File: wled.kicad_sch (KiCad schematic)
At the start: 12 parts, among them J0 Screw_Terminal_01x02, J1 Signal_Output_01, J3 1Wire_output_02, J4 1Wire_output_01, J5 I2C_output_01, SW1 Button_01, SW2 Button_Reset, U1 NodeMCU_1.0_(ESP-12E)

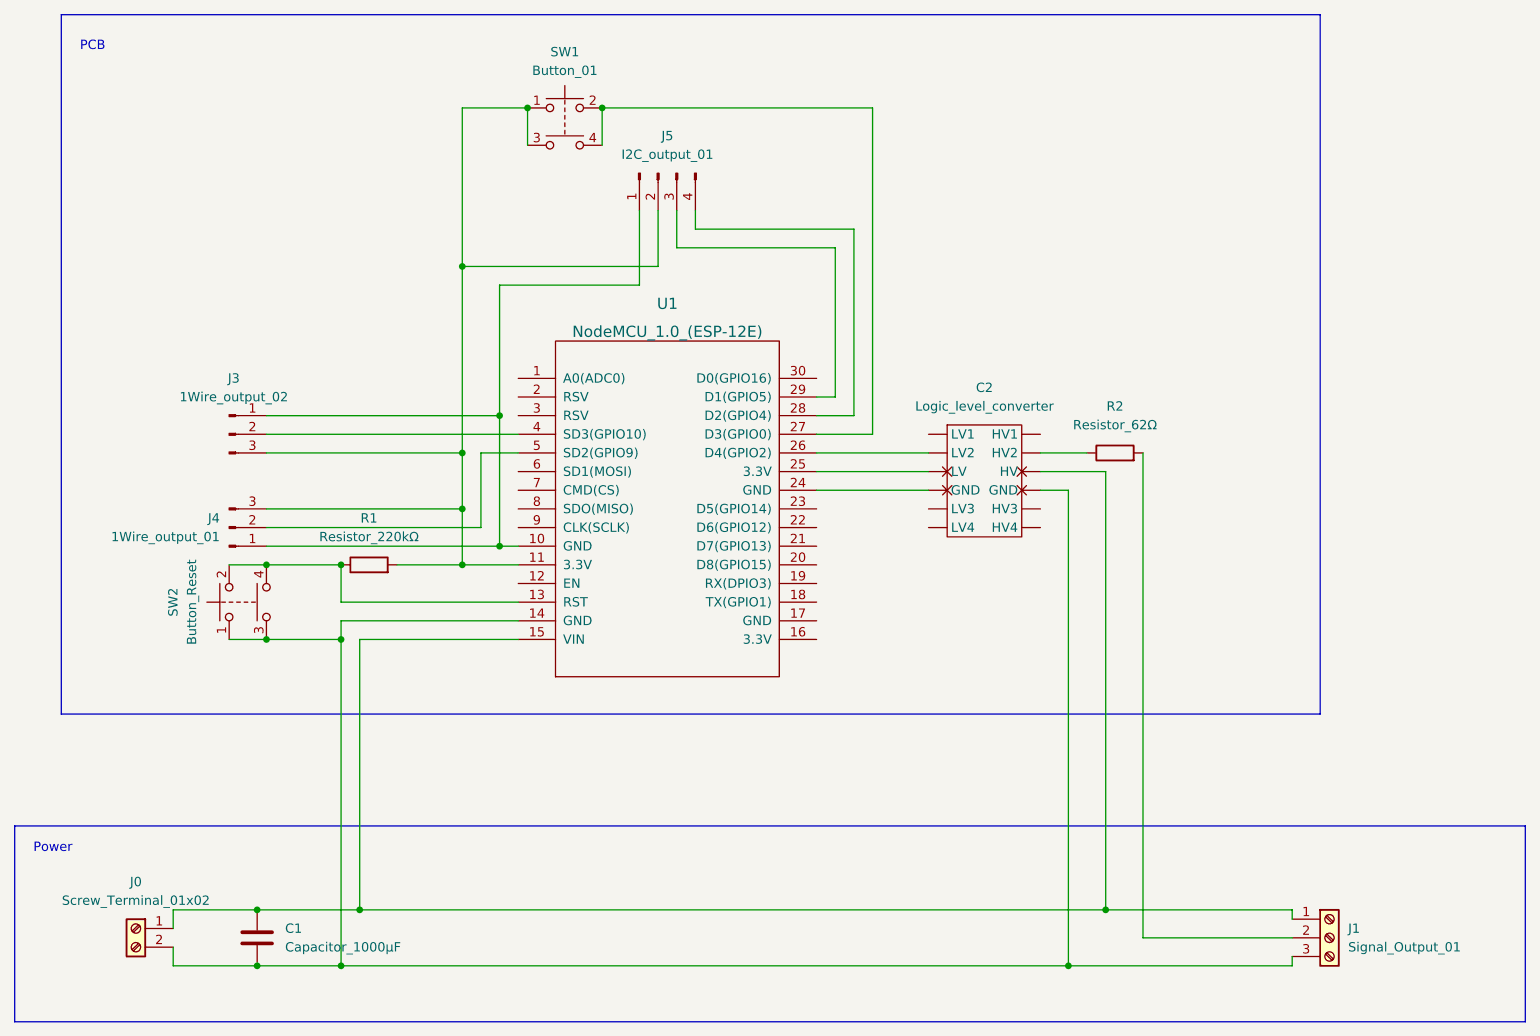
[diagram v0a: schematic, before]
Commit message: feat: Updated PCB design
This is a Release Candidate version of the board. It still has some issues, and they will be fixed in the next commit
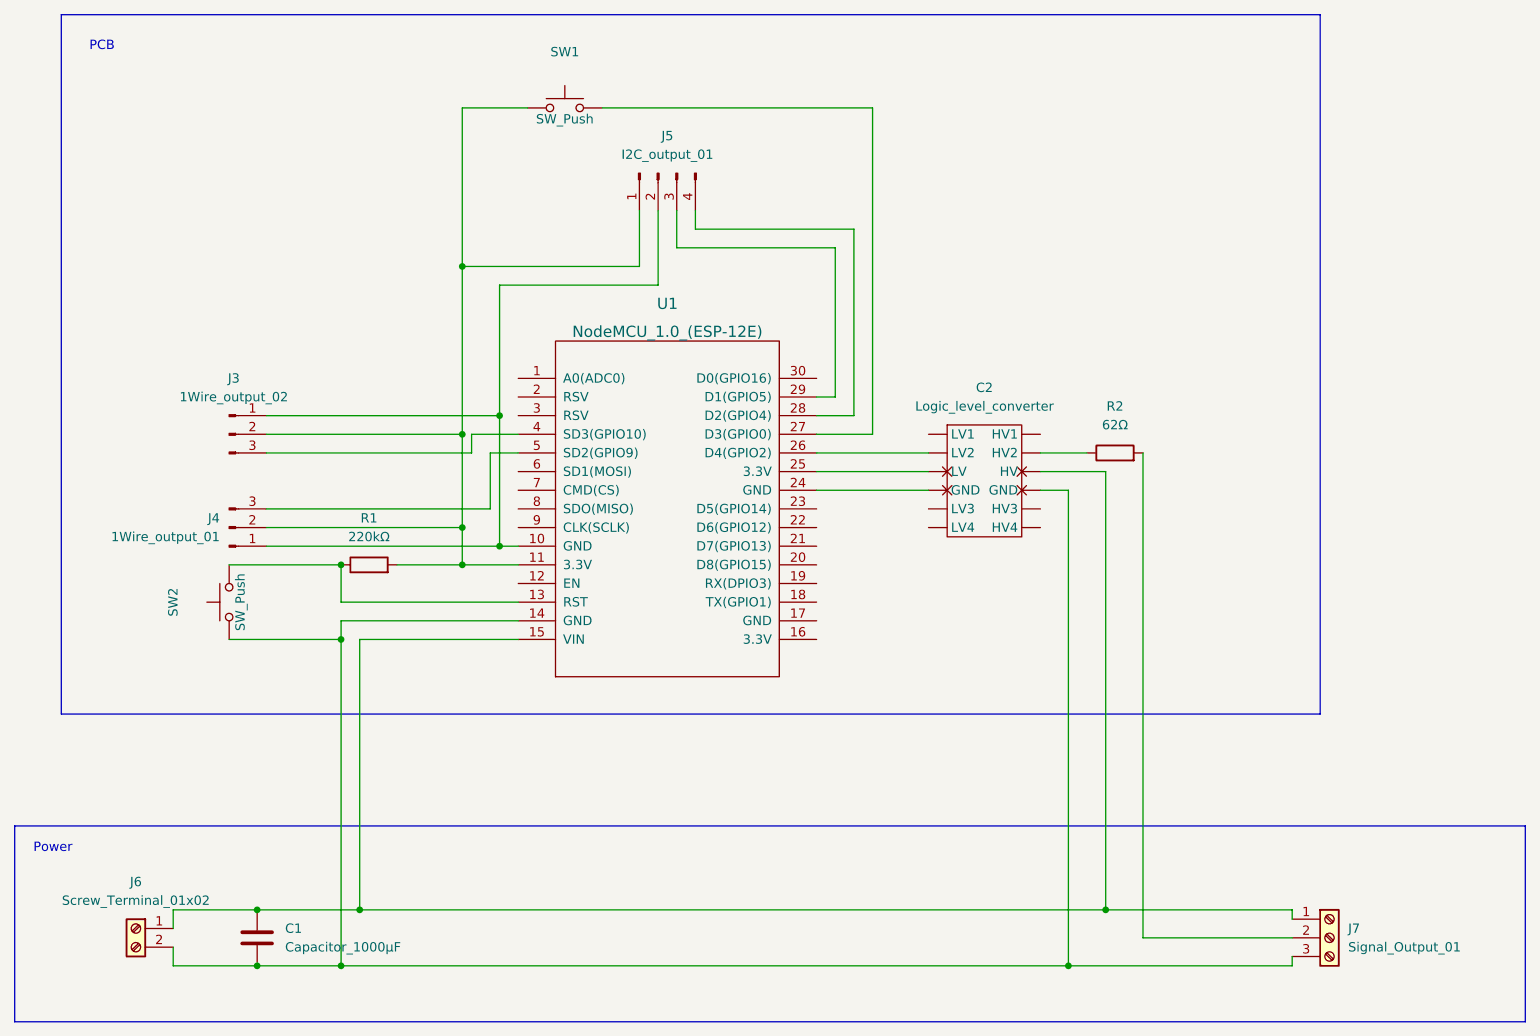
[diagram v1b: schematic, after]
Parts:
- C1: now left out of the parts list
- J6: renamed from J0; now left out of the parts list
- J7: renamed from J1; now left out of the parts list
- R1: value Resistor_220kΩ -> 220kΩ
- R2: value Resistor_62Ω -> 62Ω
- SW1: value Button_01 -> SW_Push; symbol Switch:SW_Push_Dual -> Switch:SW_Push
- SW2: value Button_Reset -> SW_Push; symbol Switch:SW_Push_Dual -> Switch:SW_Push
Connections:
- net at C1.2, C2.10 (GND), J6.2 (Pin_2)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: no longer SW2.3
- net at J3.1 (Pin_1), J4.1 (Pin_1), U1.10 (GND): now also J5.2 (Pin_2); no longer J5.1 (Pin_1)
- net at J3.2 (Pin_2): now also J4.2 (Pin_2), J5.1 (Pin_1), R1.2, SW1.1, U1.11 (3.3V); no longer U1.4 (SD3(GPIO10))
- net at SW1.2, U1.27 (D3(GPIO0)): no longer SW1.4
- net at R1.1, SW2.2, U1.13 (RST): no longer SW2.4
- net at U1.5 (SD2(GPIO9)): now also J4.3 (Pin_3); no longer J4.2 (Pin_2)
- new net: J3.3 (Pin_3), U1.4 (SD3(GPIO10))

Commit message: feat: Migrated project to KiCad 7.0
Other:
- moved on the sheet: R1
